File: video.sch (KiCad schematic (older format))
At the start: 32 parts, among them CN10 COMPOSITE, CN9 VIDEO_DB23M, U4 DENISE, U40 74LS245, U41 74LS245

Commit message: Begin adding part numbers
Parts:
- C4, C40, C41: Cost (none) -> 0.078; MFG Name (none) -> KEMET; MFG Part Num (none) -> C412C334M5U5TA; Optional (none) -> VIDEO
- C403: MFG Name (none) -> SKIP; MFG Part Num (none) -> SKIP
- CN10, CN9, U40, U41: Optional (none) -> VIDEO
- HY1, HY2: MFG Name (none) -> SKIP; MFG Part Num (none) -> SKIP; Optional (none) -> VID
- JP11: MFG Name (none) -> SKIP; MFG Part Num (none) -> SKIP; Optional (none) -> JMP
- R402, R403, R404: Optional (none) -> ROM
- U4: Optional (none) -> CUSTOM
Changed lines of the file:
@@
 F 2 "Package_DIP:DIP-48_W15.24mm_Socket_LongPads" H 3435 3625 50  0001 C CNN
 F 3 "DOCUMENTATION" H 3435 3625 50  0001 C CNN
+F 4 "CUSTOM" H 3435 3625 50  0001 C CNN "Optional"
 	1    3435 3625
 	1    0    0    -1
@@
 F 2 "Raemixx500:VariCap" H 2080 5515 50  0001 C CNN
 F 3 "~" H 2080 5515 50  0001 C CNN
+F 4 "SKIP" H 2080 5515 50  0001 C CNN "MFG Name"
+F 5 "SKIP" H 2080 5515 50  0001 C CNN "MFG Part Num"
 	1    2080 5515
 	1    0    0    -1
@@
 F 2 "Package_DIP:DIP-20_W7.62mm_Socket_LongPads" H 5330 3475 50  0001 C CNN
 F 3 "http://www.ti.com/lit/gpn/sn74LS245" H 5330 3475 50  0001 C CNN
+F 4 "VIDEO" H 5330 3475 50  0001 C CNN "Optional"
 	1    5330 3475
 	1    0    0    -1
@@
 F 2 "Package_DIP:DIP-20_W7.62mm_Socket_LongPads" H 5330 4775 50  0001 C CNN
 F 3 "http://www.ti.com/lit/gpn/sn74LS245" H 5330 4775 50  0001 C CNN
+F 4 "VIDEO" H 5330 4775 50  0001 C CNN "Optional"
 	1    5330 4775
 	1    0    0    -1
@@
 F 2 "Connector_PinHeader_2.54mm:PinHeader_1x22_P2.54mm_Vertical" H 7540 3675 50  0001 C CNN
 F 3 "DOCUMENTATION" H 7540 3675 50  0001 C CNN
+F 4 "SKIP" H 7540 3675 50  0001 C CNN "MFG Name"
+F 5 "SKIP" H 7540 3675 50  0001 C CNN "MFG Part Num"
+F 6 "VID" H 7540 3675 50  0001 C CNN "Optional"
 	1    7540 3675
 	1    0    0    -1
@@
 F 2 "Raemixx500:DB_23M" H 14680 4565 50  0001 C CNN
 F 3 " ~" H 14680 4565 50  0001 C CNN
+F 4 "VIDEO" H 14680 4565 50  0001 C CNN "Optional"
 	1    14680 4565
 	1    0    0    -1
@@
 F 2 "Raemixx500:R_Axial_DIN0309_L9.0mm_D3.2mm_P12.70mm_Horizontal" V 12480 3120 50  0001 C CNN
 F 3 "~" H 12550 3120 50  0001 C CNN
+F 4 "ROM" H 12550 3120 50  0001 C CNN "Optional"
 	1    12550 3120
 	1    0    0    -1
@@
 F 2 "Raemixx500:R_Axial_DIN0309_L9.0mm_D3.2mm_P12.70mm_Horizontal" V 12675 3120 50  0001 C CNN
 F 3 "~" H 12745 3120 50  0001 C CNN
+F 4 "ROM" H 12745 3120 50  0001 C CNN "Optional"
 	1    12745 3120
 	1    0    0    -1
@@
 F 2 "Raemixx500:R_Axial_DIN0309_L9.0mm_D3.2mm_P12.70mm_Horizontal" V 12865 3115 50  0001 C CNN
 F 3 "~" H 12935 3115 50  0001 C CNN
+F 4 "ROM" H 12935 3115 50  0001 C CNN "Optional"
 	1    12935 3115
 	1    0    0    -1
@@
 F 2 "Package_DIP:DIP-20_W7.62mm_Socket_LongPads" H 5950 8200 50  0001 C CNN
 F 3 "http://www.ti.com/lit/gpn/sn74LS245" H 5950 8200 50  0001 C CNN
+F 4 "VIDEO" H 5950 8200 50  0001 C CNN "Optional"
 	2    5950 8200
 	1    0    0    -1
@@
 F 2 "Package_DIP:DIP-20_W7.62mm_Socket_LongPads" H 7450 8200 50  0001 C CNN
 F 3 "http://www.ti.com/lit/gpn/sn74LS245" H 7450 8200 50  0001 C CNN
+F 4 "VIDEO" H 7450 8200 50  0001 C CNN "Optional"
 	2    7450 8200
 	1    0    0    -1
@@
 F 2 "Connector_PinHeader_2.54mm:PinHeader_1x22_P2.54mm_Vertical" H 8900 8200 50  0001 C CNN
 F 3 "DOCUMENTATION" H 8900 8200 50  0001 C CNN
+F 4 "SKIP" H 8900 8200 50  0001 C CNN "MFG Name"
+F 5 "SKIP" H 8900 8200 50  0001 C CNN "MFG Part Num"
+F 6 "VID" H 8900 8200 50  0001 C CNN "Optional"
 	2    8900 8200
 	-1   0    0    -1
@@
 F 2 "Package_DIP:DIP-48_W15.24mm_Socket_LongPads" H 3550 8150 50  0001 C CNN
 F 3 "DOCUMENTATION" H 3550 8150 50  0001 C CNN
+F 4 "CUSTOM" H 3550 8150 50  0001 C CNN "Optional"
 	2    3550 8150
 	1    0    0    -1
@@
 F 2 "Raemixx500:C_Axial_L6.3mm_D2.5mm_P10.16mm" H 4288 8050 50  0001 C CNN
 F 3 "~" H 4250 8200 50  0001 C CNN
+F 4 "KEMET" H 4250 8200 50  0001 C CNN "MFG Name"
+F 5 "C412C334M5U5TA" H 4250 8200 50  0001 C CNN "MFG Part Num"
+F 6 "0.078" H 4250 8200 50  0001 C CNN "Cost"
+F 7 "VIDEO" H 4250 8200 50  0001 C CNN "Optional"
 	1    4250 8200
 	1    0    0    -1
@@
 F 2 "Raemixx500:C_Axial_L6.3mm_D2.5mm_P10.16mm" H 6788 8050 50  0001 C CNN
 F 3 "~" H 6750 8200 50  0001 C CNN
+F 4 "KEMET" H 6750 8200 50  0001 C CNN "MFG Name"
+F 5 "C412C334M5U5TA" H 6750 8200 50  0001 C CNN "MFG Part Num"
+F 6 "0.078" H 6750 8200 50  0001 C CNN "Cost"
+F 7 "VIDEO" H 6750 8200 50  0001 C CNN "Optional"
 	1    6750 8200
 	1    0    0    -1
@@
 F 2 "Raemixx500:C_Axial_L6.3mm_D2.5mm_P10.16mm" H 8238 8050 50  0001 C CNN
 F 3 "~" H 8200 8200 50  0001 C CNN
+F 4 "KEMET" H 8200 8200 50  0001 C CNN "MFG Name"
+F 5 "C412C334M5U5TA" H 8200 8200 50  0001 C CNN "MFG Part Num"
+F 6 "0.078" H 8200 8200 50  0001 C CNN "Cost"
+F 7 "VIDEO" H 8200 8200 50  0001 C CNN "Optional"
 	1    8200 8200
 	1    0    0    -1
@@
 F 2 "Raemixx500:Jumper3-Bridged12" H 8635 4570 50  0001 C CNN
 F 3 "~" H 8635 4570 50  0001 C CNN
+F 4 "SKIP" H 8635 4570 50  0001 C CNN "MFG Name"
+F 5 "SKIP" H 8635 4570 50  0001 C CNN "MFG Part Num"
+F 6 "JMP" H 8635 4570 50  0001 C CNN "Optional"
 	1    8635 4570
 	0    -1   -1   0
@@
 F 2 "Connector_PinHeader_2.54mm:PinHeader_1x03_P2.54mm_Vertical" H 7540 5390 50  0001 C CNN
 F 3 "https://github.com/SukkoPera/OpenAmigaVideoHybrid" H 7540 5390 50  0001 C CNN
+F 4 "SKIP" H 7540 5390 50  0001 C CNN "MFG Name"
+F 5 "SKIP" H 7540 5390 50  0001 C CNN "MFG Part Num"
+F 6 "VID" H 7540 5390 50  0001 C CNN "Optional"
 	1    7540 5390
 	1    0    0    -1
@@
 F 5 "13mm" H 10280 4175 50  0001 L BNN "Field5"
 F 6 "Manufacturer Recommendations" H 10280 4175 50  0001 L BNN "Field6"
+F 7 "VIDEO" H 10280 4175 50  0001 C CNN "Optional"
 	1    10280 4175
 	-1   0    0    -1

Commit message: More part numbers
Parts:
- R402, R403, R404: Optional ROM -> (none)
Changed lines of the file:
@@
 F 2 "Raemixx500:R_Axial_DIN0309_L9.0mm_D3.2mm_P12.70mm_Horizontal" V 12480 3120 50  0001 C CNN
 F 3 "~" H 12550 3120 50  0001 C CNN
-F 4 "ROM" H 12550 3120 50  0001 C CNN "Optional"
+F 4 "" H 12550 3120 50  0001 C CNN "Optional"
 	1    12550 3120
 	1    0    0    -1
@@
 F 2 "Raemixx500:R_Axial_DIN0309_L9.0mm_D3.2mm_P12.70mm_Horizontal" V 12675 3120 50  0001 C CNN
 F 3 "~" H 12745 3120 50  0001 C CNN
-F 4 "ROM" H 12745 3120 50  0001 C CNN "Optional"
+F 4 "" H 12745 3120 50  0001 C CNN "Optional"
 	1    12745 3120
 	1    0    0    -1
@@
 F 2 "Raemixx500:R_Axial_DIN0309_L9.0mm_D3.2mm_P12.70mm_Horizontal" V 12865 3115 50  0001 C CNN
 F 3 "~" H 12935 3115 50  0001 C CNN
-F 4 "ROM" H 12935 3115 50  0001 C CNN "Optional"
+F 4 "" H 12935 3115 50  0001 C CNN "Optional"
 	1    12935 3115
 	1    0    0    -1

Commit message: Use 12.5mm footprints for C401/2 - Closes #16
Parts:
- C401, C402: footprint Capacitor_THT:CP_Radial_D8.0mm_P5.00mm -> Capacitor_THT:CP_Radial_D12.5mm_P5.00mm
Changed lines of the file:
@@
 F 0 "C402" H 5265 8246 50  0000 L CNN
 F 1 "1000u" H 5265 8155 50  0000 L CNN
-F 2 "Capacitor_THT:CP_Radial_D8.0mm_P5.00mm" H 5150 8200 50  0001 C CNN
+F 2 "Capacitor_THT:CP_Radial_D12.5mm_P5.00mm" H 5150 8200 50  0001 C CNN
 F 3 "~" H 5150 8200 50  0001 C CNN
 	1    5150 8200
@@
 F 0 "C401" H 9740 8246 50  0000 L CNN
 F 1 "1000u" H 9740 8155 50  0000 L CNN
-F 2 "Capacitor_THT:CP_Radial_D8.0mm_P5.00mm" H 9625 8200 50  0001 C CNN
+F 2 "Capacitor_THT:CP_Radial_D12.5mm_P5.00mm" H 9625 8200 50  0001 C CNN
 F 3 "~" H 9625 8200 50  0001 C CNN
 	1    9625 8200

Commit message: More part numbers
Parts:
- C401, C402: Cost (none) -> 0.343; MFG Name (none) -> PANASONIC; MFG Part Num (none) -> EEUFR1C102
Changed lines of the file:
@@
 F 2 "Capacitor_THT:CP_Radial_D12.5mm_P5.00mm" H 5150 8200 50  0001 C CNN
 F 3 "~" H 5150 8200 50  0001 C CNN
+F 4 "PANASONIC" H 5150 8200 50  0001 C CNN "MFG Name"
+F 5 "0.343" H 5150 8200 50  0001 C CNN "Cost"
+F 6 "EEUFR1C102" H 5150 8200 50  0001 C CNN "MFG Part Num"
 	1    5150 8200
 	1    0    0    -1
@@
 F 2 "Capacitor_THT:CP_Radial_D12.5mm_P5.00mm" H 9625 8200 50  0001 C CNN
 F 3 "~" H 9625 8200 50  0001 C CNN
+F 4 "PANASONIC" H 9625 8200 50  0001 C CNN "MFG Name"
+F 5 "0.343" H 9625 8200 50  0001 C CNN "Cost"
+F 6 "EEUFR1C102" H 9625 8200 50  0001 C CNN "MFG Part Num"
 	1    9625 8200
 	1    0    0    -1

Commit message: Guess what???
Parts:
- U40, U41: Cost (none) -> 0.311; MFG Name (none) -> TI; MFG Part Num (none) -> CD74ACT245E
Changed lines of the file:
@@
 F 3 "http://www.ti.com/lit/gpn/sn74LS245" H 5330 3475 50  0001 C CNN
 F 4 "VIDEO" H 5330 3475 50  0001 C CNN "Optional"
+F 5 "0.311" H 5330 3475 50  0001 C CNN "Cost"
+F 6 "TI" H 5330 3475 50  0001 C CNN "MFG Name"
+F 7 "CD74ACT245E" H 5330 3475 50  0001 C CNN "MFG Part Num"
 	1    5330 3475
 	1    0    0    -1
@@
 F 3 "http://www.ti.com/lit/gpn/sn74LS245" H 5330 4775 50  0001 C CNN
 F 4 "VIDEO" H 5330 4775 50  0001 C CNN "Optional"
+F 5 "0.311" H 5330 4775 50  0001 C CNN "Cost"
+F 6 "TI" H 5330 4775 50  0001 C CNN "MFG Name"
+F 7 "CD74ACT245E" H 5330 4775 50  0001 C CNN "MFG Part Num"
 	1    5330 4775
 	1    0    0    -1
@@
 F 3 "http://www.ti.com/lit/gpn/sn74LS245" H 5950 8200 50  0001 C CNN
 F 4 "VIDEO" H 5950 8200 50  0001 C CNN "Optional"
+F 5 "0.311" H 5950 8200 50  0001 C CNN "Cost"
+F 6 "TI" H 5950 8200 50  0001 C CNN "MFG Name"
+F 7 "CD74ACT245E" H 5950 8200 50  0001 C CNN "MFG Part Num"
 	2    5950 8200
 	1    0    0    -1
@@
 F 3 "http://www.ti.com/lit/gpn/sn74LS245" H 7450 8200 50  0001 C CNN
 F 4 "VIDEO" H 7450 8200 50  0001 C CNN "Optional"
+F 5 "0.311" H 7450 8200 50  0001 C CNN "Cost"
+F 6 "TI" H 7450 8200 50  0001 C CNN "MFG Name"
+F 7 "CD74ACT245E" H 7450 8200 50  0001 C CNN "MFG Part Num"
 	2    7450 8200
 	1    0    0    -1

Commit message: Add EMI filter types
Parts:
- E402, E434: EMI_FILTER_TYPE (none) -> W/FERRITE; Optional (none) -> VIDEO
- E403, E404, E405, E406: EMI_FILTER_TYPE (none) -> W/FERRITE
- E431, E432, E433, E435: EMI_FILTER_TYPE (none) -> FERRITE; Optional (none) -> VIDEO
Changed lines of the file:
@@
 F 2 "Raemixx500:EMI_Filter_Long" V 14655 3185 50  0001 C CNN
 F 3 "http://www.murata.com/~/media/webrenewal/support/library/catalog/products/emc/emifil/c31e.ashx?la=en-gb" V 14655 3185 50  0001 C CNN
+F 4 "W/FERRITE" H 14655 3185 50  0001 C CNN "EMI_FILTER_TYPE"
 	1    14655 3185
 	-1   0    0    -1
@@
 F 2 "Raemixx500:EMI_Filter_Long" V 14430 2445 50  0001 C CNN
 F 3 "http://www.murata.com/~/media/webrenewal/support/library/catalog/products/emc/emifil/c31e.ashx?la=en-gb" V 14430 2445 50  0001 C CNN
+F 4 "W/FERRITE" H 14430 2445 50  0001 C CNN "EMI_FILTER_TYPE"
 	1    14430 2445
 	-1   0    0    -1
@@
 F 2 "Raemixx500:EMI_Filter_Long" V 14540 2805 50  0001 C CNN
 F 3 "http://www.murata.com/~/media/webrenewal/support/library/catalog/products/emc/emifil/c31e.ashx?la=en-gb" V 14540 2805 50  0001 C CNN
+F 4 "W/FERRITE" H 14540 2805 50  0001 C CNN "EMI_FILTER_TYPE"
 	1    14540 2805
 	-1   0    0    -1
@@
 F 2 "Raemixx500:EMI_Filter_Long" V 13000 5940 50  0001 C CNN
 F 3 "http://www.murata.com/~/media/webrenewal/support/library/catalog/products/emc/emifil/c31e.ashx?la=en-gb" V 13000 5940 50  0001 C CNN
+F 4 "W/FERRITE" H 13000 5940 50  0001 C CNN "EMI_FILTER_TYPE"
+F 5 "VIDEO" H 13000 5940 50  0001 C CNN "Optional"
 	1    13000 5940
 	1    0    0    -1
@@
 F 2 "Raemixx500:EMI_Filter_Long" V 13460 2470 50  0001 C CNN
 F 3 "http://www.murata.com/~/media/webrenewal/support/library/catalog/products/emc/emifil/c31e.ashx?la=en-gb" V 13460 2470 50  0001 C CNN
+F 4 "W/FERRITE" H 13460 2470 50  0001 C CNN "EMI_FILTER_TYPE"
+F 5 "VIDEO" H 13460 2470 50  0001 C CNN "Optional"
 	1    13460 2470
 	1    0    0    -1
@@
 F 2 "Raemixx500:EMI_Filter_Short" V 3450 7200 50  0001 C CNN
 F 3 "http://www.murata.com/~/media/webrenewal/support/library/catalog/products/emc/emifil/c31e.ashx?la=en-gb" V 3450 7200 50  0001 C CNN
+F 4 "W/FERRITE" H 3450 7200 50  0001 C CNN "EMI_FILTER_TYPE"
 	1    3450 7200
 	0    1    1    0
@@
 F 2 "Raemixx500:EMI_Filter_Long" V 12100 5065 50  0001 C CNN
 F 3 "http://www.murata.com/~/media/webrenewal/support/library/catalog/products/emc/emifil/c31e.ashx?la=en-gb" V 12100 5065 50  0001 C CNN
+F 4 "FERRITE" H 12100 5065 50  0001 C CNN "EMI_FILTER_TYPE"
+F 5 "VIDEO" H 12100 5065 50  0001 C CNN "Optional"
 	1    12100 5065
 	1    0    0    -1
@@
 F 2 "Raemixx500:EMI_Filter_Long" V 12100 5465 50  0001 C CNN
 F 3 "http://www.murata.com/~/media/webrenewal/support/library/catalog/products/emc/emifil/c31e.ashx?la=en-gb" V 12100 5465 50  0001 C CNN
+F 4 "FERRITE" H 12100 5465 50  0001 C CNN "EMI_FILTER_TYPE"
+F 5 "VIDEO" H 12100 5465 50  0001 C CNN "Optional"
 	1    12100 5465
 	1    0    0    -1
@@
 F 2 "Raemixx500:EMI_Filter_Long" V 11450 5265 50  0001 C CNN
 F 3 "http://www.murata.com/~/media/webrenewal/support/library/catalog/products/emc/emifil/c31e.ashx?la=en-gb" V 11450 5265 50  0001 C CNN
+F 4 "FERRITE" H 11450 5265 50  0001 C CNN "EMI_FILTER_TYPE"
+F 5 "VIDEO" H 11450 5265 50  0001 C CNN "Optional"
 	1    11450 5265
 	1    0    0    -1
@@
 F 2 "Raemixx500:EMI_Filter_Long" V 9120 4075 50  0001 C CNN
 F 3 "http://www.murata.com/~/media/webrenewal/support/library/catalog/products/emc/emifil/c31e.ashx?la=en-gb" V 9120 4075 50  0001 C CNN
+F 4 "FERRITE" H 9120 4075 50  0001 C CNN "EMI_FILTER_TYPE"
+F 5 "VIDEO" H 9120 4075 50  0001 C CNN "Optional"
 	1    9120 4075
 	1    0    0    -1

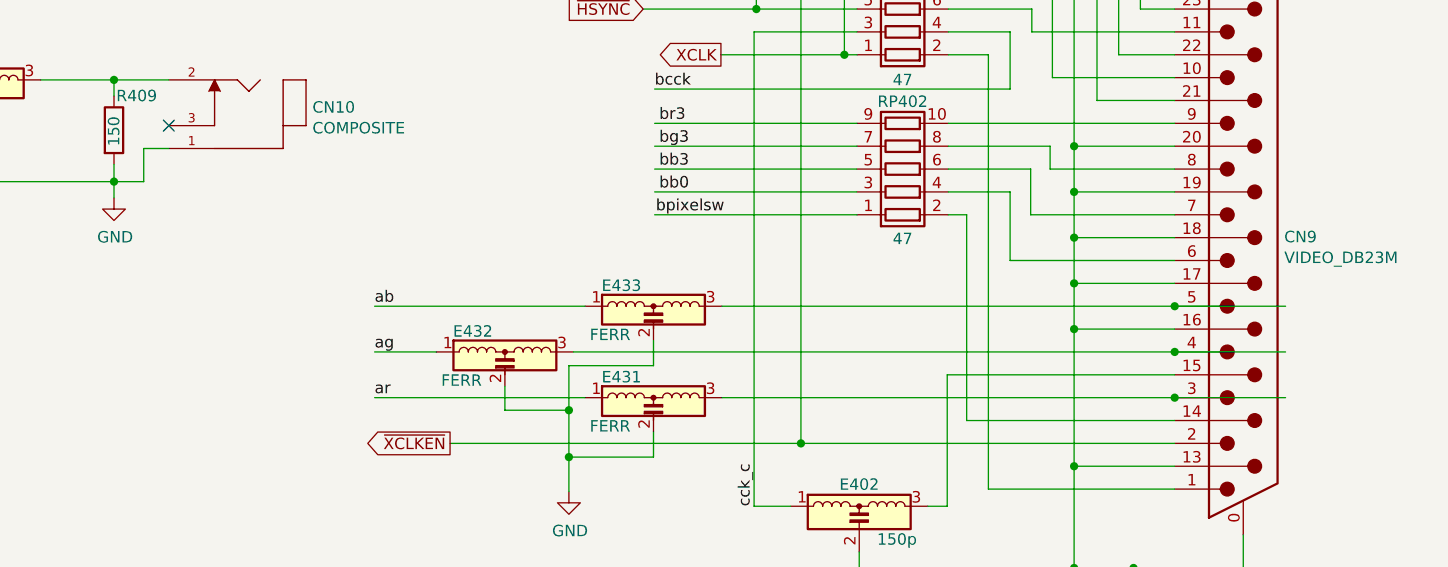
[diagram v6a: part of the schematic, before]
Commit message: Add part numbers for EMI filters Not the original filters, but what seem to be suitable replacements available today
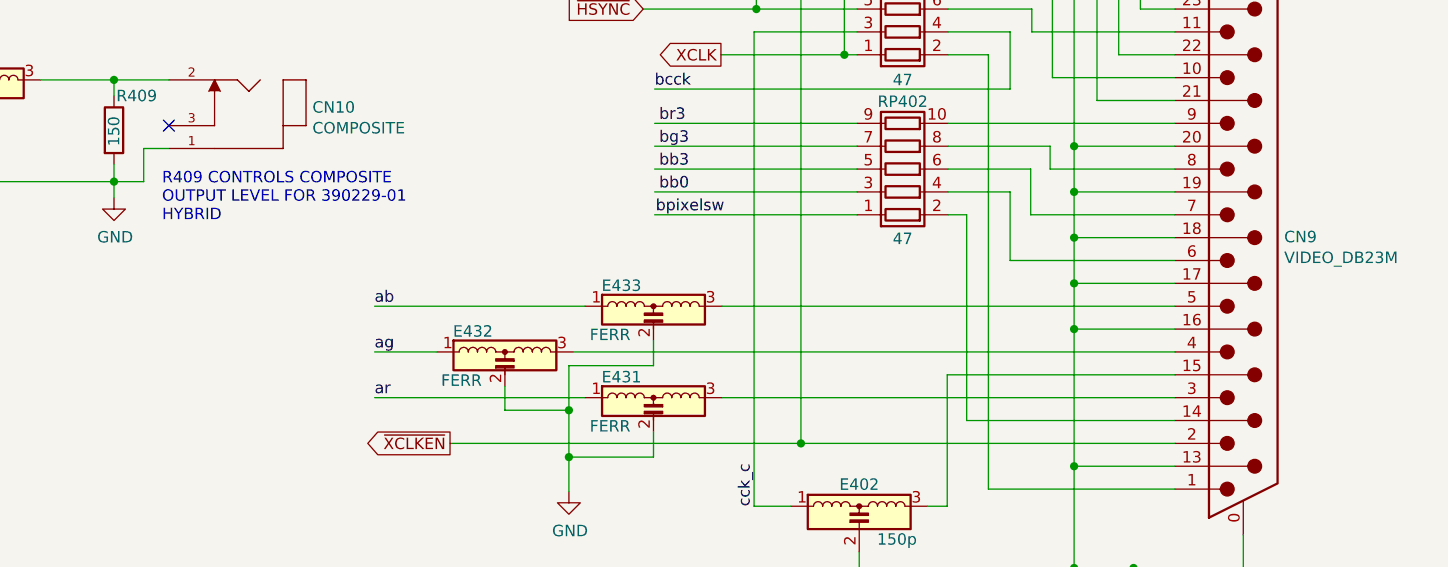
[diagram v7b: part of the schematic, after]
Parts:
- E402, E434: Cost (none) -> 0.238; MFG Name (none) -> MURATA; MFG Part Num (none) -> DSS1NB32A151Q91A
- E403, E404, E405, E406: Cost (none) -> 0.234; MFG Name (none) -> MURATA; MFG Part Num (none) -> DSS1NB32A151Q91A
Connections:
- wire segments 317 -> 314
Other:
- note added: "R409 CONTROLS COMPOSITE\nOUTPUT LEVEL FOR 390229-01\nHYBRID"
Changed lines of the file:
@@
 F 3 "http://www.murata.com/~/media/webrenewal/support/library/catalog/products/emc/emifil/c31e.ashx?la=en-gb" V 14655 3185 50  0001 C CNN
 F 4 "W/FERRITE" H 14655 3185 50  0001 C CNN "EMI_FILTER_TYPE"
+F 5 "0.234" H 14655 3185 50  0001 C CNN "Cost"
+F 6 "MURATA" H 14655 3185 50  0001 C CNN "MFG Name"
+F 7 "DSS1NB32A151Q91A" H 14655 3185 50  0001 C CNN "MFG Part Num"
 	1    14655 3185
 	-1   0    0    -1
@@
 F 3 "http://www.murata.com/~/media/webrenewal/support/library/catalog/products/emc/emifil/c31e.ashx?la=en-gb" V 14430 2445 50  0001 C CNN
 F 4 "W/FERRITE" H 14430 2445 50  0001 C CNN "EMI_FILTER_TYPE"
+F 5 "0.234" H 14430 2445 50  0001 C CNN "Cost"
+F 6 "MURATA" H 14430 2445 50  0001 C CNN "MFG Name"
+F 7 "DSS1NB32A151Q91A" H 14430 2445 50  0001 C CNN "MFG Part Num"
 	1    14430 2445
 	-1   0    0    -1
@@
 F 3 "http://www.murata.com/~/media/webrenewal/support/library/catalog/products/emc/emifil/c31e.ashx?la=en-gb" V 14540 2805 50  0001 C CNN
 F 4 "W/FERRITE" H 14540 2805 50  0001 C CNN "EMI_FILTER_TYPE"
+F 5 "0.234" H 14540 2805 50  0001 C CNN "Cost"
+F 6 "MURATA" H 14540 2805 50  0001 C CNN "MFG Name"
+F 7 "DSS1NB32A151Q91A" H 14540 2805 50  0001 C CNN "MFG Part Num"
 	1    14540 2805
 	-1   0    0    -1
@@
 F 4 "W/FERRITE" H 13000 5940 50  0001 C CNN "EMI_FILTER_TYPE"
 F 5 "VIDEO" H 13000 5940 50  0001 C CNN "Optional"
+F 6 "0.238" H 13000 5940 50  0001 C CNN "Cost"
+F 7 "MURATA" H 13000 5940 50  0001 C CNN "MFG Name"
+F 8 "DSS1NB32A151Q91A " H 13000 5940 50  0001 C CNN "MFG Part Num"
 	1    13000 5940
 	1    0    0    -1
@@
 F 4 "W/FERRITE" H 13460 2470 50  0001 C CNN "EMI_FILTER_TYPE"
 F 5 "VIDEO" H 13460 2470 50  0001 C CNN "Optional"
+F 6 "0.238" H 13460 2470 50  0001 C CNN "Cost"
+F 7 "MURATA" H 13460 2470 50  0001 C CNN "MFG Name"
+F 8 "DSS1NB32A151Q91A " H 13460 2470 50  0001 C CNN "MFG Part Num"
 	1    13460 2470
 	1    0    0    -1
@@
 F 3 "http://www.murata.com/~/media/webrenewal/support/library/catalog/products/emc/emifil/c31e.ashx?la=en-gb" V 3450 7200 50  0001 C CNN
 F 4 "W/FERRITE" H 3450 7200 50  0001 C CNN "EMI_FILTER_TYPE"
+F 5 "0.234" H 3450 7200 50  0001 C CNN "Cost"
+F 6 "MURATA" H 3450 7200 50  0001 C CNN "MFG Name"
+F 7 "DSS1NB32A151Q91A" H 3450 7200 50  0001 C CNN "MFG Part Num"
 	1    3450 7200
 	0    1    1    0
@@
 Text GLabel 11210 5565 0    50   Output ~ 0
 ~XCLKEN
-Connection ~ 14380 4965
-Wire Wire Line
-	14380 4965 14865 4965
-Connection ~ 14380 5165
-Wire Wire Line
-	14380 5165 14865 5165
-Connection ~ 14380 5365
-Wire Wire Line
-	14380 5365 14865 5365
 Wire Wire Line
 	12100 5115 12100 5225
@@
 Wire Bus Line
 	2005 2075 2005 3575
+Text Notes 9950 4600 0    50   ~ 0
+R409 CONTROLS COMPOSITE\nOUTPUT LEVEL FOR 390229-01\nHYBRID
 $EndSCHEMATC
